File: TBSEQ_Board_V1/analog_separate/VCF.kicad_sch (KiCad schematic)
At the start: 66 parts, among them Q10 PNP, Q11 NPN, Q12 HN4C06J-BL_6P DIP, Q13 NPN, Q14 NPN, Q15 NPN, Q16 NPN, Q17 NPN, Q18 NPN, Q19 NPN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

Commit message: replace
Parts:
- added J3: Conn_01x02_Pin, Connector_PinHeader_2.54mm:PinHeader_1x02_P2.54mm_Vertical, symbol Connector:Conn_01x02_Pin
- C13, C14, C15, C17, C22, C23, C29: footprint Capacitor_THT:CP_Radial_D6.3mm_P2.50mm -> Capacitor_THT:CP_Radial_D5.0mm_P2.00mm
- C16, C28, C30: footprint Capacitor_THT:CP_Radial_D6.3mm_P2.50mm -> Capacitor_THT:CP_Radial_D4.0mm_P2.00mm
- D24: footprint Diode_THT:D_DO-15_P10.16mm_Horizontal -> Diode_THT:D_A-405_P2.54mm_Vertical_AnodeUp
- Q12, Q21: footprint SamacSys_Parts:HN4C06JBLTE85LF -> Package_DIP:DIP-6_W7.62mm
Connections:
- net A+VCA_Resonance: now also J3.2 (Pin_2)
- net A+VCA_Signal: now also J3.1 (Pin_1)
- net at C17.2, Q12.1 (B1), R70.1: no longer R68.1, R98.2
- net at C16.1, R70.2: now also R68.1, R98.2
- net A+VCO_MIX renamed A+VCO_WAVE
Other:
- note added: "toVCA"
- moved on the sheet: C16, R68, R98

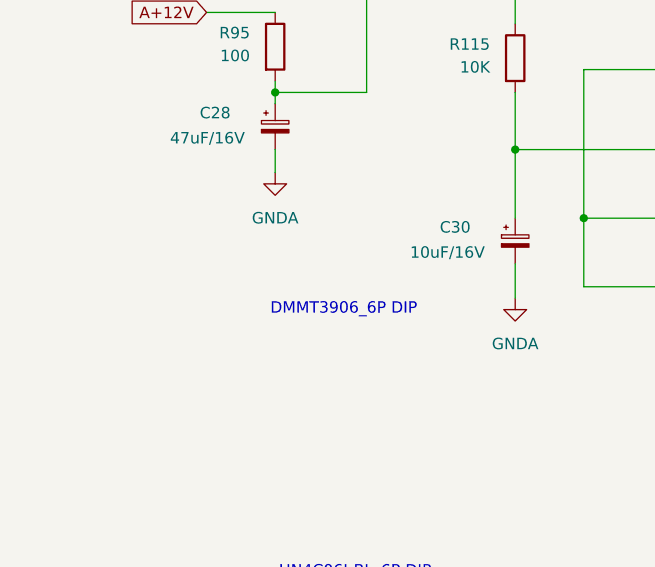
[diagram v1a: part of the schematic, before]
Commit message: analog_separate Fix
DMMT3906->HN4C51J
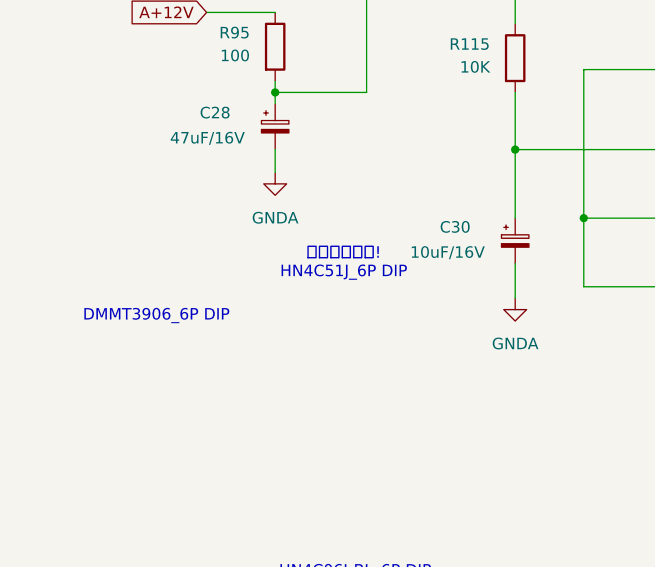
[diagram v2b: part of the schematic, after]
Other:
- note added: "こっちが正解! HN4C51J_6P DIP"
